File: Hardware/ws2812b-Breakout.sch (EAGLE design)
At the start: 11 parts

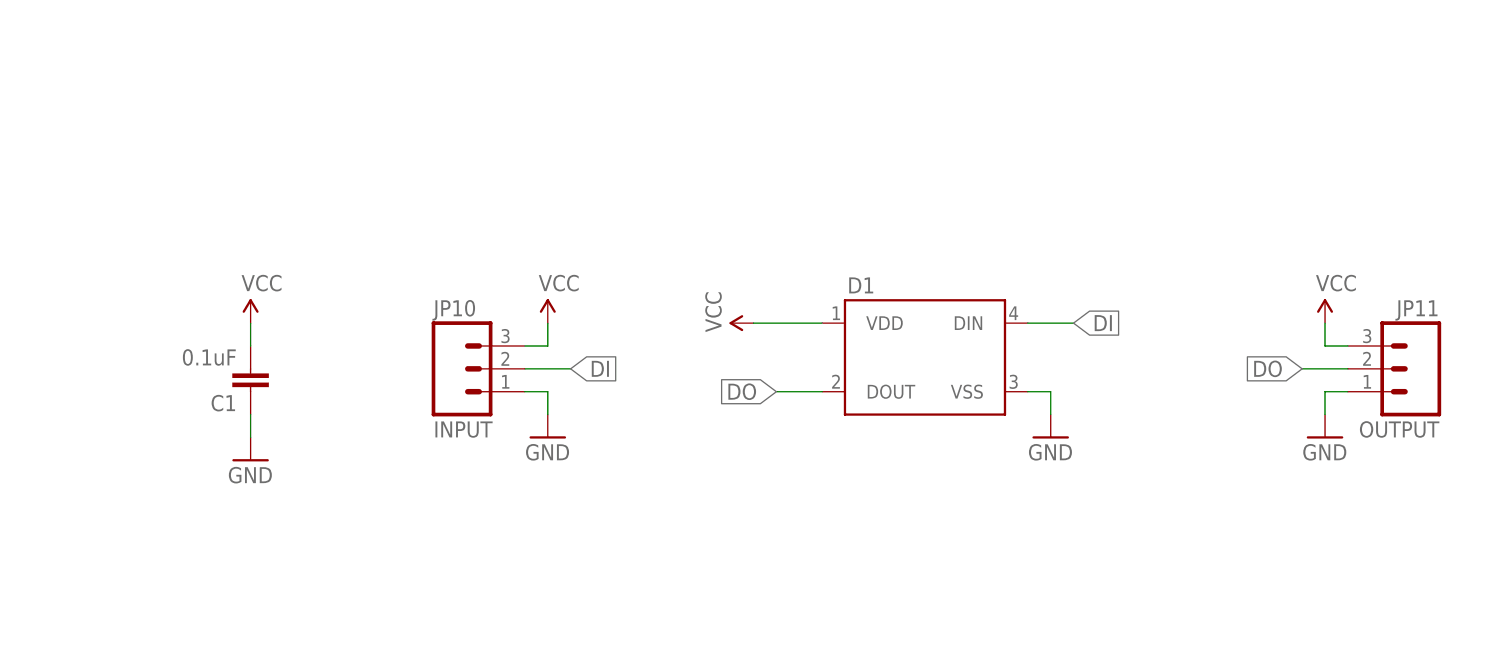
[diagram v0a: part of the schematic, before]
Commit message: Updated Frame / LED package.
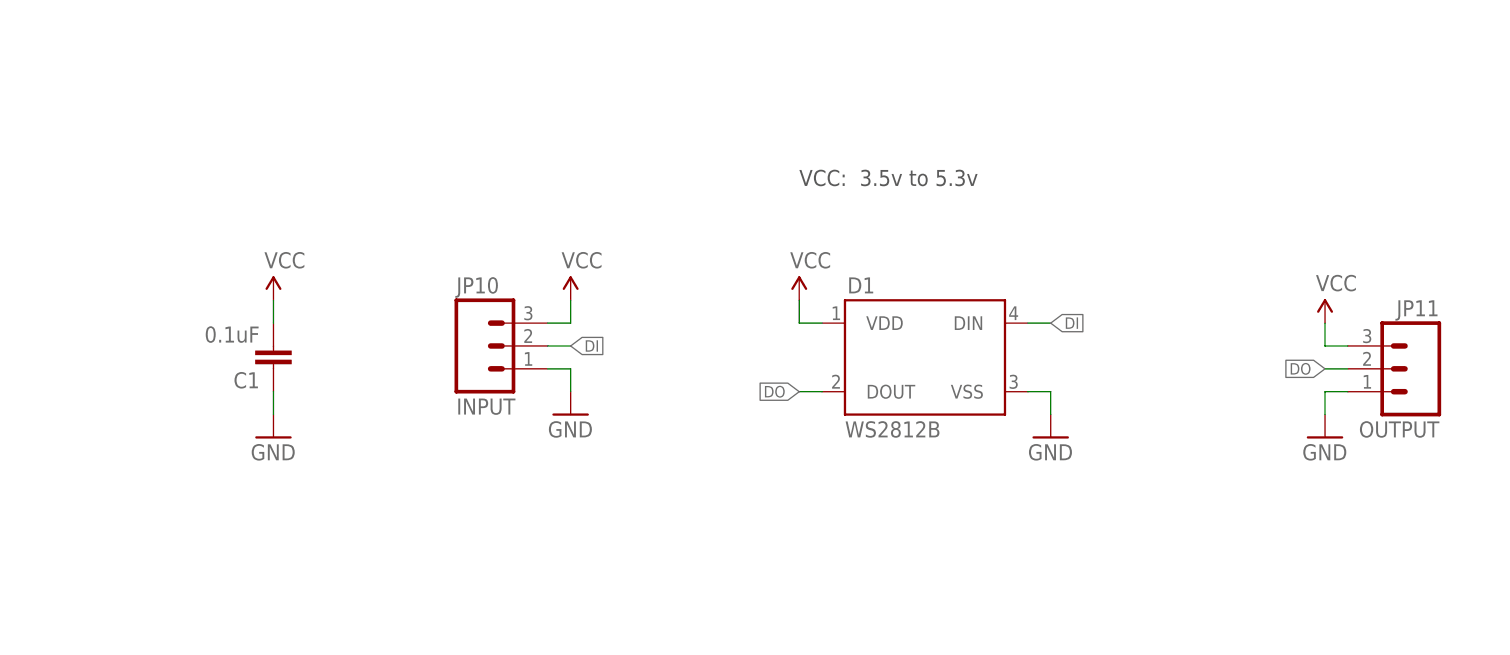
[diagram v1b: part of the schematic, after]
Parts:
- D1: value (none) -> WS2812B
- FRAME1: value FRAME-LETTER -> (none)
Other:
- note added: "VCC: 3.5v to 5.3v"
- moved on the sheet: C1, JP10
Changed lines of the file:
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@@
 <layer number="56" name="wert" color="7" fill="1" visible="no" active="no"/>
 <layer number="57" name="tCAD" color="7" fill="1" visible="no" active="no"/>
+<layer number="90" name="Modules" color="5" fill="1" visible="yes" active="yes"/>
 <layer number="91" name="Nets" color="2" fill="1" visible="yes" active="yes"/>
 <layer number="92" name="Busses" color="1" fill="1" visible="yes" active="yes"/>
@@
 <layer number="111" name="LPC17xx" color="7" fill="1" visible="yes" active="yes"/>
 <layer number="112" name="tSilk" color="7" fill="1" visible="yes" active="yes"/>
+<layer number="113" name="IDFDebug" color="4" fill="1" visible="yes" active="yes"/>
 <layer number="116" name="Patch_BOT" color="9" fill="4" visible="yes" active="yes"/>
 <layer number="121" name="_tsilk" color="7" fill="1" visible="yes" active="yes"/>
@@
 <part name="FID1" library="SparkFun-Aesthetics" deviceset="FIDUCIAL" device="UFIDUCIAL"/>
 <part name="FID2" library="SparkFun-Aesthetics" deviceset="FIDUCIAL" device="UFIDUCIAL"/>
-<part name="D1" library="SparkFun-LED" deviceset="WS2812B" device=""/>
+<part name="D1" library="SparkFun-LED" deviceset="WS2812B" device="" value="WS2812B"/>
 <part name="P+2" library="SparkFun" deviceset="VCC" device=""/>
 <part name="GND5" library="SparkFun" deviceset="GND" device=""/>
@@
 <text x="170.434" y="10.922" size="2.54" layer="94">N. Seidle</text>
 <text x="148.59" y="6.604" size="2.54" layer="94">Revised by: Patrick Alberts</text>
+<text x="101.6" y="127" size="1.778" layer="97">VCC:  3.5v to 5.3v</text>
 </plain>
 <instances>
-<instance part="FRAME1" gate="G$1" x="0" y="0"/>
-<instance part="FRAME1" gate="G$2" x="147.32" y="0"/>
-<instance part="P+1" gate="1" x="40.64" y="111.76"/>
-<instance part="GND1" gate="1" x="40.64" y="96.52"/>
-<instance part="C1" gate="G$1" x="40.64" y="106.68" rot="R180"/>
+<instance part="FRAME1" gate="G$1" x="0" y="0" smashed="yes"/>
+<instance part="FRAME1" gate="V" x="147.32" y="0" smashed="yes">
+<attribute name="LAST_DATE_TIME" x="160.02" y="1.27" size="2.54" layer="94" font="vector"/>
+<attribute name="SHEET" x="233.68" y="1.27" size="2.54" layer="94" font="vector"/>
+<attribute name="DRAWING_NAME" x="162.814" y="17.78" size="2.7432" layer="94" font="vector"/>
+</instance>
+<instance part="P+1" gate="1" x="43.18" y="114.3" smashed="yes">
+<attribute name="VALUE" x="42.164" y="117.856" size="1.778" layer="96"/>
+</instance>
+<instance part="GND1" gate="1" x="43.18" y="99.06" smashed="yes">
+<attribute name="VALUE" x="40.64" y="96.52" size="1.778" layer="96"/>
+</instance>
+<instance part="C1" gate="G$1" x="43.18" y="109.22" smashed="yes" rot="R180">
+<attribute name="NAME" x="41.656" y="106.299" size="1.778" layer="95" rot="R180"/>
+<attribute name="VALUE" x="41.656" y="111.379" size="1.778" layer="96" rot="R180"/>
+</instance>
 <instance part="JP1" gate="G$1" x="246.38" y="33.02"/>
 <instance part="JP4" gate="G$1" x="241.3" y="33.02"/>
-<instance part="JP10" gate="G$1" x="63.5" y="106.68"/>
+<instance part="JP10" gate="G$1" x="66.04" y="109.22" smashed="yes">
+<attribute name="VALUE" x="63.5" y="101.6" size="1.778" layer="96"/>
+<attribute name="NAME" x="63.5" y="115.062" size="1.778" layer="95"/>
+</instance>
 <instance part="JP11" gate="G$1" x="170.18" y="106.68" rot="MR0"/>
-<instance part="P+4" gate="1" x="73.66" y="111.76"/>
-<instance part="GND3" gate="1" x="73.66" y="99.06"/>
+<instance part="P+4" gate="1" x="76.2" y="114.3" smashed="yes">
+<attribute name="VALUE" x="75.184" y="117.856" size="1.778" layer="96"/>
+</instance>
+<instance part="GND3" gate="1" x="76.2" y="101.6" smashed="yes">
+<attribute name="VALUE" x="73.66" y="99.06" size="1.778" layer="96"/>
+</instance>
 <instance part="P+5" gate="1" x="160.02" y="111.76"/>
 <instance part="GND4" gate="1" x="160.02" y="99.06"/>
@@
 <instance part="FID2" gate="G$1" x="246.38" y="27.94"/>
 <instance part="D1" gate="G$1" x="109.22" y="106.68"/>
-<instance part="P+2" gate="1" x="96.52" y="111.76" rot="R90"/>
+<instance part="P+2" gate="1" x="101.6" y="114.3"/>
 <instance part="GND5" gate="1" x="129.54" y="99.06"/>
 <instance part="LOGO2" gate="G$1" x="210.82" y="40.64"/>
@@
 <net name="VCC" class="0">
 <segment>
-<wire x1="40.64" y1="111.76" x2="40.64" y2="109.22" width="0.1524" layer="91"/>
+<wire x1="43.18" y1="114.3" x2="43.18" y2="111.76" width="0.1524" layer="91"/>
 <pinref part="P+1" gate="1" pin="VCC"/>
 <pinref part="C1" gate="G$1" pin="2"/>
@@
 <pinref part="JP10" gate="G$1" pin="3"/>
 <pinref part="P+4" gate="1" pin="VCC"/>
-<wire x1="71.12" y1="109.22" x2="73.66" y2="109.22" width="0.1524" layer="91"/>
-<wire x1="73.66" y1="109.22" x2="73.66" y2="111.76" width="0.1524" layer="91"/>
+<wire x1="73.66" y1="111.76" x2="76.2" y2="111.76" width="0.1524" layer="91"/>
+<wire x1="76.2" y1="111.76" x2="76.2" y2="114.3" width="0.1524" layer="91"/>
 </segment>
 <segment>
@@
 <segment>
 <pinref part="P+2" gate="1" pin="VCC"/>
-<wire x1="104.14" y1="111.76" x2="96.52" y2="111.76" width="0.1524" layer="91"/>
+<wire x1="104.14" y1="111.76" x2="101.6" y2="111.76" width="0.1524" layer="91"/>
+<wire x1="101.6" y1="111.76" x2="101.6" y2="114.3" width="0.1524" layer="91"/>
 <pinref part="D1" gate="G$1" pin="VDD"/>
 </segment>
@@
 <net name="GND" class="0">
 <segment>
-<wire x1="40.64" y1="101.6" x2="40.64" y2="99.06" width="0.1524" layer="91"/>
+<wire x1="43.18" y1="104.14" x2="43.18" y2="101.6" width="0.1524" layer="91"/>
 <pinref part="GND1" gate="1" pin="GND"/>
 <pinref part="C1" gate="G$1" pin="1"/>
@@
 <pinref part="JP10" gate="G$1" pin="1"/>
 <pinref part="GND3" gate="1" pin="GND"/>
-<wire x1="71.12" y1="104.14" x2="73.66" y2="104.14" width="0.1524" layer="91"/>
-<wire x1="73.66" y1="104.14" x2="73.66" y2="101.6" width="0.1524" layer="91"/>
+<wire x1="73.66" y1="106.68" x2="76.2" y2="106.68" width="0.1524" layer="91"/>
+<wire x1="76.2" y1="106.68" x2="76.2" y2="104.14" width="0.1524" layer="91"/>
 </segment>
 <segment>
@@
 <segment>
 <pinref part="JP11" gate="G$1" pin="2"/>
-<wire x1="162.56" y1="106.68" x2="157.48" y2="106.68" width="0.1524" layer="91"/>
-<label x="157.48" y="106.68" size="1.778" layer="95" rot="R180" xref="yes"/>
-</segment>
-<segment>
-<label x="99.06" y="104.14" size="1.778" layer="95" rot="R180" xref="yes"/>
+<wire x1="162.56" y1="106.68" x2="160.02" y2="106.68" width="0.1524" layer="91"/>
+<label x="160.02" y="106.68" size="1.27" layer="95" rot="R180" xref="yes"/>
+</segment>
+<segment>
+<label x="101.6" y="104.14" size="1.27" layer="95" rot="R180" xref="yes"/>
 <pinref part="D1" gate="G$1" pin="DOUT"/>
-<wire x1="104.14" y1="104.14" x2="99.06" y2="104.14" width="0.1524" layer="91"/>
+<wire x1="104.14" y1="104.14" x2="101.6" y2="104.14" width="0.1524" layer="91"/>
 </segment>
 </net>
@@
 <segment>
 <pinref part="JP10" gate="G$1" pin="2"/>
-<wire x1="71.12" y1="106.68" x2="76.2" y2="106.68" width="0.1524" layer="91"/>
-<label x="76.2" y="106.68" size="1.778" layer="95" xref="yes"/>
-</segment>
-<segment>
-<wire x1="127" y1="111.76" x2="132.08" y2="111.76" width="0.1524" layer="91"/>
-<label x="132.08" y="111.76" size="1.778" layer="95" xref="yes"/>
+<wire x1="73.66" y1="109.22" x2="76.2" y2="109.22" width="0.1524" layer="91"/>
+<label x="76.2" y="109.22" size="1.27" layer="95" xref="yes"/>
+</segment>
+<segment>
+<wire x1="127" y1="111.76" x2="129.54" y2="111.76" width="0.1524" layer="91"/>
+<label x="129.54" y="111.76" size="1.27" layer="95" xref="yes"/>
 <pinref part="D1" gate="G$1" pin="DIN"/>
 </segment>

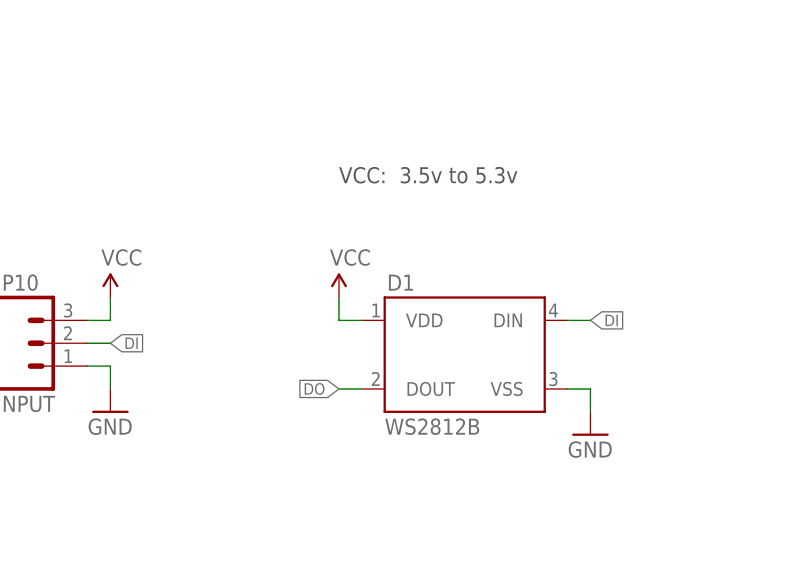
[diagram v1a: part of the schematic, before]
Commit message: qc checklist items fixed
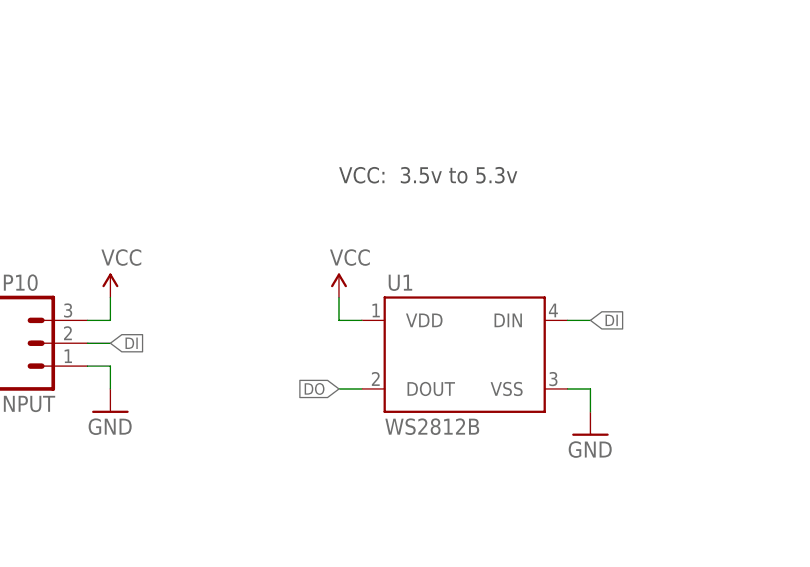
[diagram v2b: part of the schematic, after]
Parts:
- renumbered D1 to U1
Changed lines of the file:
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@@
 <?xml version="1.0" encoding="utf-8"?>
 <!DOCTYPE eagle SYSTEM "eagle.dtd">
-<eagle version="6.4">
+<eagle version="7.2.0">
 <drawing>
 <settings>
@@
 <part name="FID1" library="SparkFun-Aesthetics" deviceset="FIDUCIAL" device="UFIDUCIAL"/>
 <part name="FID2" library="SparkFun-Aesthetics" deviceset="FIDUCIAL" device="UFIDUCIAL"/>
-<part name="D1" library="SparkFun-LED" deviceset="WS2812B" device="" value="WS2812B"/>
+<part name="U1" library="SparkFun-LED" deviceset="WS2812B" device="" value="WS2812B"/>
 <part name="P+2" library="SparkFun" deviceset="VCC" device=""/>
 <part name="GND5" library="SparkFun" deviceset="GND" device=""/>
@@
 <instance part="FID1" gate="G$1" x="241.3" y="27.94"/>
 <instance part="FID2" gate="G$1" x="246.38" y="27.94"/>
-<instance part="D1" gate="G$1" x="109.22" y="106.68"/>
+<instance part="U1" gate="G$1" x="109.22" y="106.68"/>
 <instance part="P+2" gate="1" x="101.6" y="114.3"/>
 <instance part="GND5" gate="1" x="129.54" y="99.06"/>
@@
 <wire x1="104.14" y1="111.76" x2="101.6" y2="111.76" width="0.1524" layer="91"/>
 <wire x1="101.6" y1="111.76" x2="101.6" y2="114.3" width="0.1524" layer="91"/>
-<pinref part="D1" gate="G$1" pin="VDD"/>
+<pinref part="U1" gate="G$1" pin="VDD"/>
 </segment>
 </net>
@@
 <wire x1="127" y1="104.14" x2="129.54" y2="104.14" width="0.1524" layer="91"/>
 <wire x1="129.54" y1="104.14" x2="129.54" y2="101.6" width="0.1524" layer="91"/>
-<pinref part="D1" gate="G$1" pin="VSS"/>
+<pinref part="U1" gate="G$1" pin="VSS"/>
 </segment>
 </net>
@@
 <segment>
 <label x="101.6" y="104.14" size="1.27" layer="95" rot="R180" xref="yes"/>
-<pinref part="D1" gate="G$1" pin="DOUT"/>
+<pinref part="U1" gate="G$1" pin="DOUT"/>
 <wire x1="104.14" y1="104.14" x2="101.6" y2="104.14" width="0.1524" layer="91"/>
 </segment>
@@
 <wire x1="127" y1="111.76" x2="129.54" y2="111.76" width="0.1524" layer="91"/>
 <label x="129.54" y="111.76" size="1.27" layer="95" xref="yes"/>
-<pinref part="D1" gate="G$1" pin="DIN"/>
-</segment>
-</net>
+<pinref part="U1" gate="G$1" pin="DIN"/>
+</segment>
+</net>

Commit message: Fixed qc issues
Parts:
- removed JP10: INPUT, SparkFun-Connectors:M03PTH
- added JP15: STAND-OFF, SparkFun:STAND-OFF
- JP1: value STAND-OFF -> INPUT; device SparkFun:STAND-OFF -> SparkFun-Connectors:M03PTH
- renumbered JP11 to JP2
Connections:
- net DI: now also JP1.2; no longer JP10.2
- net GND: now also JP1.1; no longer JP10.1
- net VCC: now also JP1.3; no longer JP10.3
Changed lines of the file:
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@@
 <part name="GND1" library="SparkFun" deviceset="GND" device=""/>
 <part name="C1" library="SparkFun-Capacitors" deviceset="0.1UF-25V(+80/-20%)(0603)" device="" value="0.1uF"/>
-<part name="JP1" library="SparkFun" deviceset="STAND-OFF" device=""/>
+<part name="JP15" library="SparkFun" deviceset="STAND-OFF" device=""/>
 <part name="JP4" library="SparkFun" deviceset="STAND-OFF" device=""/>
-<part name="JP10" library="SparkFun-Connectors" deviceset="M03" device="PTH" value="INPUT"/>
-<part name="JP11" library="SparkFun-Connectors" deviceset="M03" device="PTH" value="OUTPUT"/>
+<part name="JP1" library="SparkFun-Connectors" deviceset="M03" device="PTH" value="INPUT"/>
+<part name="JP2" library="SparkFun-Connectors" deviceset="M03" device="PTH" value="OUTPUT"/>
 <part name="P+4" library="SparkFun" deviceset="VCC" device=""/>
 <part name="GND3" library="SparkFun" deviceset="GND" device=""/>
@@
 <attribute name="VALUE" x="41.656" y="111.379" size="1.778" layer="96" rot="R180"/>
 </instance>
-<instance part="JP1" gate="G$1" x="246.38" y="33.02"/>
+<instance part="JP15" gate="G$1" x="246.38" y="33.02"/>
 <instance part="JP4" gate="G$1" x="241.3" y="33.02"/>
-<instance part="JP10" gate="G$1" x="66.04" y="109.22" smashed="yes">
+<instance part="JP1" gate="G$1" x="66.04" y="109.22" smashed="yes">
 <attribute name="VALUE" x="63.5" y="101.6" size="1.778" layer="96"/>
 <attribute name="NAME" x="63.5" y="115.062" size="1.778" layer="95"/>
 </instance>
-<instance part="JP11" gate="G$1" x="170.18" y="106.68" rot="MR0"/>
+<instance part="JP2" gate="G$1" x="170.18" y="106.68" rot="MR0"/>
 <instance part="P+4" gate="1" x="76.2" y="114.3" smashed="yes">
 <attribute name="VALUE" x="75.184" y="117.856" size="1.778" layer="96"/>
@@
 </segment>
 <segment>
-<pinref part="JP10" gate="G$1" pin="3"/>
+<pinref part="JP1" gate="G$1" pin="3"/>
 <pinref part="P+4" gate="1" pin="VCC"/>
 <wire x1="73.66" y1="111.76" x2="76.2" y2="111.76" width="0.1524" layer="91"/>
@@
 <pinref part="P+5" gate="1" pin="VCC"/>
 <wire x1="160.02" y1="109.22" x2="160.02" y2="111.76" width="0.1524" layer="91"/>
-<pinref part="JP11" gate="G$1" pin="3"/>
+<pinref part="JP2" gate="G$1" pin="3"/>
 <wire x1="162.56" y1="109.22" x2="160.02" y2="109.22" width="0.1524" layer="91"/>
 </segment>
@@
 </segment>
 <segment>
-<pinref part="JP10" gate="G$1" pin="1"/>
+<pinref part="JP1" gate="G$1" pin="1"/>
 <pinref part="GND3" gate="1" pin="GND"/>
 <wire x1="73.66" y1="106.68" x2="76.2" y2="106.68" width="0.1524" layer="91"/>
@@
 <pinref part="GND4" gate="1" pin="GND"/>
 <wire x1="160.02" y1="104.14" x2="160.02" y2="101.6" width="0.1524" layer="91"/>
-<pinref part="JP11" gate="G$1" pin="1"/>
+<pinref part="JP2" gate="G$1" pin="1"/>
 <wire x1="162.56" y1="104.14" x2="160.02" y2="104.14" width="0.1524" layer="91"/>
 </segment>
@@
 <net name="DO" class="0">
 <segment>
-<pinref part="JP11" gate="G$1" pin="2"/>
+<pinref part="JP2" gate="G$1" pin="2"/>
 <wire x1="162.56" y1="106.68" x2="160.02" y2="106.68" width="0.1524" layer="91"/>
 <label x="160.02" y="106.68" size="1.27" layer="95" rot="R180" xref="yes"/>
@@
 <net name="DI" class="0">
 <segment>
-<pinref part="JP10" gate="G$1" pin="2"/>
+<pinref part="JP1" gate="G$1" pin="2"/>
 <wire x1="73.66" y1="109.22" x2="76.2" y2="109.22" width="0.1524" layer="91"/>
 <label x="76.2" y="109.22" size="1.27" layer="95" xref="yes"/>

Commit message: changed fids to regular size
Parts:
- FID1, FID2: value FIDUCIALUFIDUCIAL -> FIDUCIAL1X2; device SparkFun-Aesthetics:FIDUCIALUFIDUCIAL -> SparkFun-Aesthetics:FIDUCIAL1X2
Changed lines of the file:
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@@
 <?xml version="1.0" encoding="utf-8"?>
 <!DOCTYPE eagle SYSTEM "eagle.dtd">
-<eagle version="7.2.0">
+<eagle version="6.6.0">
 <drawing>
 <settings>
@@
 <part name="GND4" library="SparkFun" deviceset="GND" device=""/>
 <part name="LOGO1" library="SparkFun-Aesthetics" deviceset="OSHW-LOGO" device="S"/>
-<part name="FID1" library="SparkFun-Aesthetics" deviceset="FIDUCIAL" device="UFIDUCIAL"/>
-<part name="FID2" library="SparkFun-Aesthetics" deviceset="FIDUCIAL" device="UFIDUCIAL"/>
 <part name="U1" library="SparkFun-LED" deviceset="WS2812B" device="" value="WS2812B"/>
 <part name="P+2" library="SparkFun" deviceset="VCC" device=""/>
 <part name="GND5" library="SparkFun" deviceset="GND" device=""/>
 <part name="LOGO2" library="SparkFun-Aesthetics" deviceset="SFE_LOGO_FLAME" device=".1_INCH"/>
+<part name="FID1" library="SparkFun-Aesthetics" deviceset="FIDUCIAL" device="1X2"/>
+<part name="FID2" library="SparkFun-Aesthetics" deviceset="FIDUCIAL" device="1X2"/>
 </parts>
 <sheets>
@@
 <instance part="GND4" gate="1" x="160.02" y="99.06"/>
 <instance part="LOGO1" gate="G$1" x="233.68" y="48.26"/>
-<instance part="FID1" gate="G$1" x="241.3" y="27.94"/>
-<instance part="FID2" gate="G$1" x="246.38" y="27.94"/>
 <instance part="U1" gate="G$1" x="109.22" y="106.68"/>
 <instance part="P+2" gate="1" x="101.6" y="114.3"/>
 <instance part="GND5" gate="1" x="129.54" y="99.06"/>
 <instance part="LOGO2" gate="G$1" x="210.82" y="40.64"/>
+<instance part="FID1" gate="G$1" x="246.38" y="27.94"/>
+<instance part="FID2" gate="G$1" x="241.3" y="27.94"/>
 </instances>
 <busses>
